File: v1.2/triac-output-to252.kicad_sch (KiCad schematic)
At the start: 5 parts, among them U5 MID400

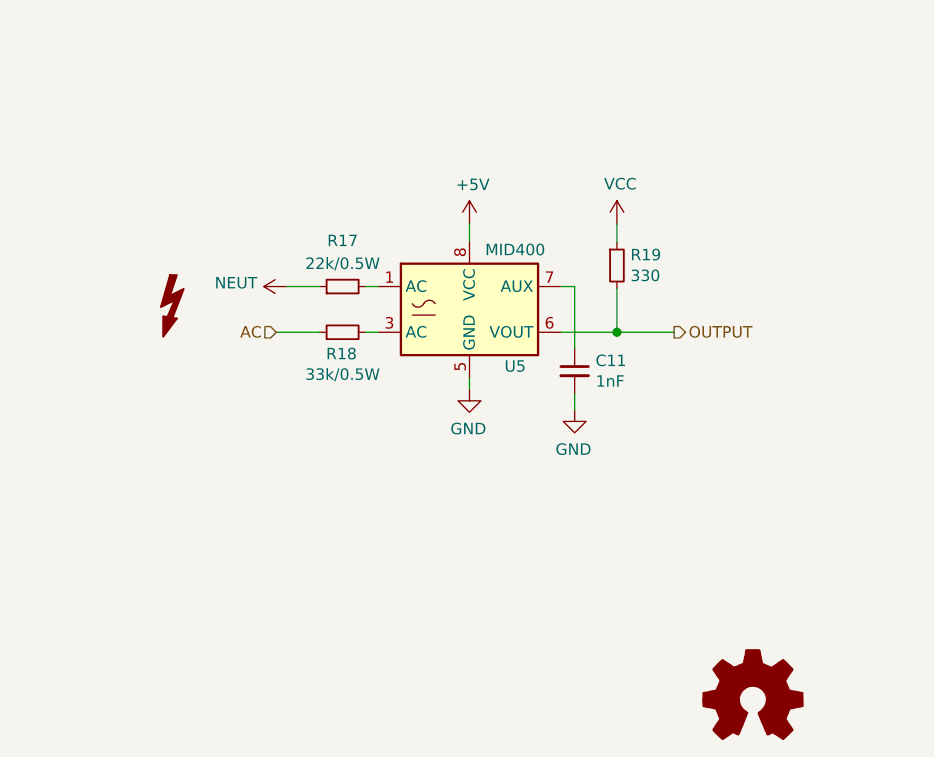
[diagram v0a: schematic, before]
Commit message: change q7 to TO263 (D2PAK) package
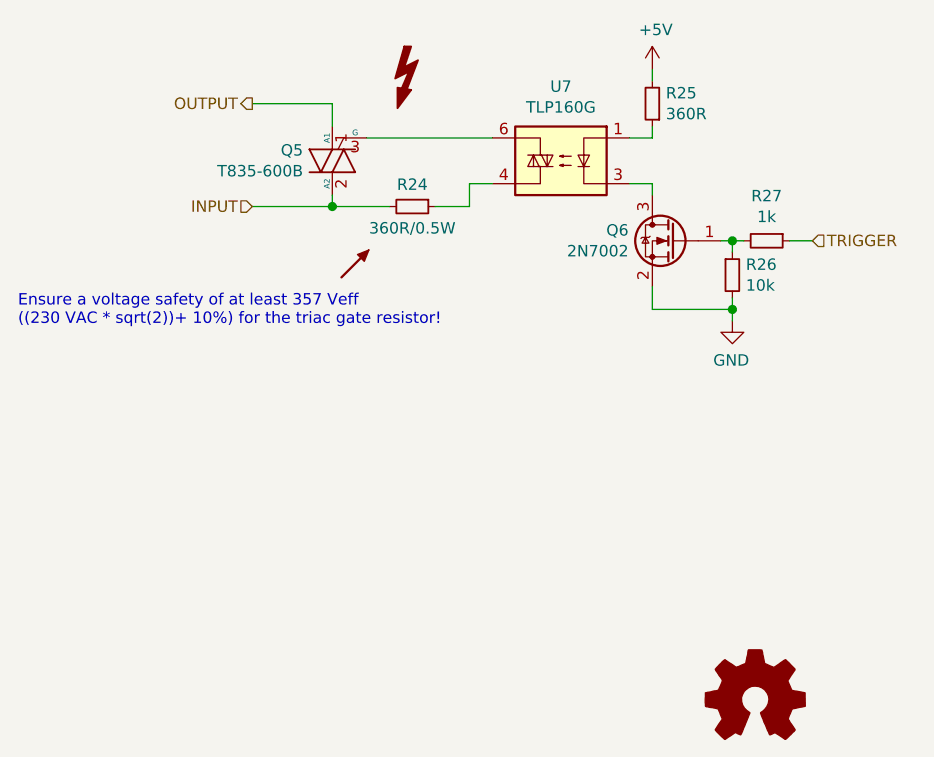
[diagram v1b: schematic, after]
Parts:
- removed C11: 1nF, Capacitor_SMD:C_0603_1608Metric_Pad1.08x0.95mm_HandSolder, symbol Device:C_Small
- removed R17: 22k/0.5W, Resistor_SMD:R_1206_3216Metric_Pad1.30x1.75mm_HandSolder, symbol Device:R_Small
- removed R18: 33k/0.5W, Resistor_SMD:R_1206_3216Metric_Pad1.30x1.75mm_HandSolder, symbol Device:R_Small
- removed R19: 330, Resistor_SMD:R_0603_1608Metric_Pad0.98x0.95mm_HandSolder, symbol Device:R_Small
- removed U5: MID400, Package_DIP:SMDIP-8_W7.62mm, symbol Isolator:MID400
- added Q5: T835-600B, Package_TO_SOT_SMD:TO-252-2, symbol Triac_Thyristor:BT138-600
- added Q6: 2N7002, Package_TO_SOT_SMD:SOT-23, symbol Transistor_FET:2N7002
- added R24: 360R/0.5W, Resistor_SMD:R_1206_3216Metric_Pad1.30x1.75mm_HandSolder, symbol Device:R_Small
- added R25: 360R, Resistor_SMD:R_0603_1608Metric_Pad0.98x0.95mm_HandSolder, symbol Device:R_Small
- added R26: 10k, Resistor_SMD:R_0603_1608Metric_Pad0.98x0.95mm_HandSolder, symbol Device:R_Small
- added R27: 1k, Resistor_SMD:R_0603_1608Metric_Pad0.98x0.95mm_HandSolder, symbol Device:R_Small
- added U7: TLP160G, Package_SO:MFSOP6-4_4.4x3.6mm_P1.27mm, symbol Relay_SolidState:TLP160G
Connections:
- net +5V: now also R25.2
- net GND: now also Q6.2 (S), R26.2
- net OUTPUT: now also Q5.1 (A1)
- new net: R25.1, U7.1
- new net: Q6.3 (D), U7.3
- new net: R24.1, U7.4
- new net: Q5.3 (G), U7.6
- new net: Q6.1 (G), R26.1, R27.2
- new net INPUT: Q5.2 (A2), R24.2
- new net TRIGGER: R27.1
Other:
- note added: "Ensure a voltage safety of at least 357 Veff ((230 VAC * sqrt(2))+ 10%) for the triac gate resistor!"
